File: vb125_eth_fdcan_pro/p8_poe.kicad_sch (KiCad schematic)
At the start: 61 parts, among them Q5 MMBTA42, Q6 Si3440DV, Q7 2N7002, T1 PA1134NL, U11 LTC4267, U12 PS2911-1-F3-AX, U13 ZR431

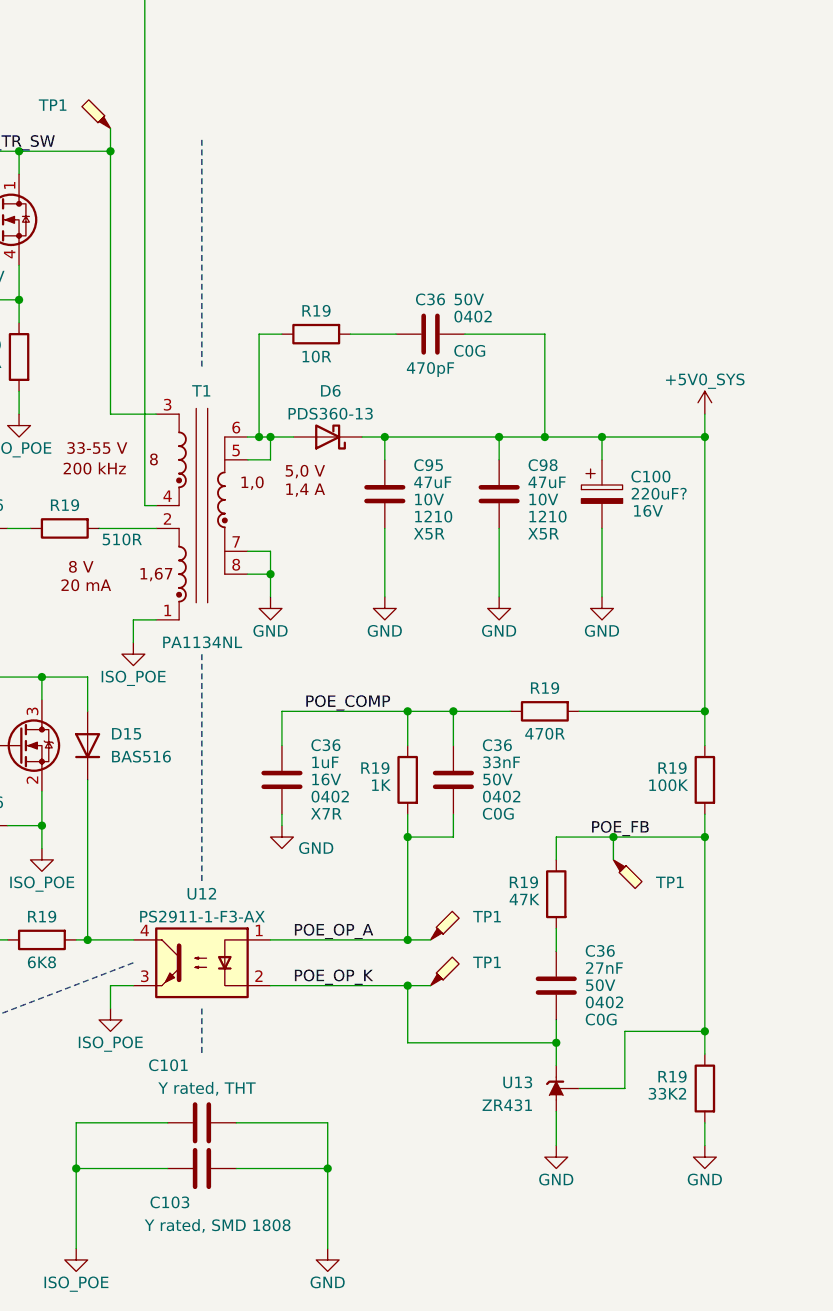
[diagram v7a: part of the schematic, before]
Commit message: Preliminary placement.
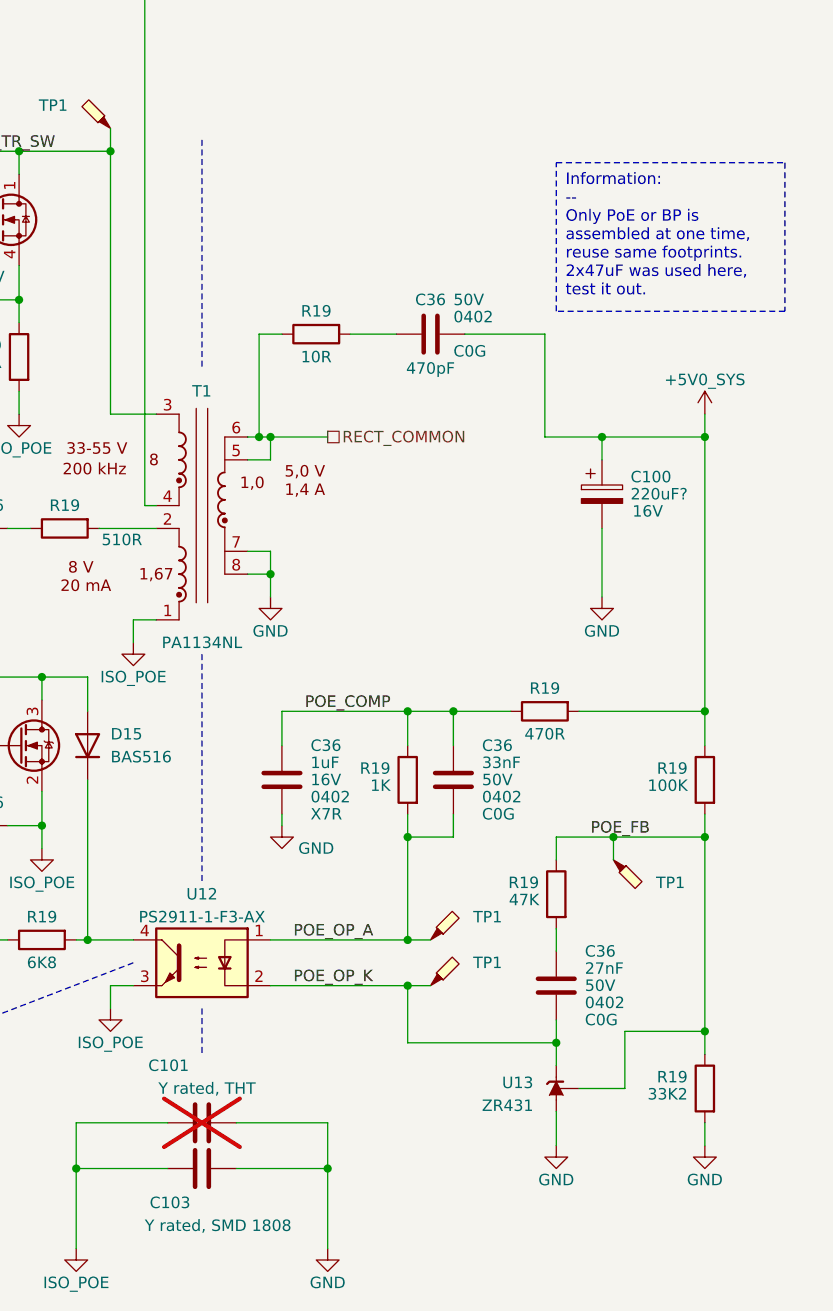
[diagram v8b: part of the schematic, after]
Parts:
- removed C95, C98: 47uF, Capacitor_SMD:C_1210_3225Metric, symbol Device:C
- removed D6: PDS360-13, Diode_SMD:D_PowerDI-5, symbol Device:D_Schottky
- C101: now not fitted; now left out of the parts list
- U12: footprint Package_DIP:DIP-4_W7.62mm -> vhrd_opto_isolator:PS2911
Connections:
- net RECT_COMMON: now reaches R19.1, T1.5, T1.6
